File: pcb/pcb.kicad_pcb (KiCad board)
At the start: 2 copper layers, 234.7 x 91.6 mm, 95 parts, among them J1 USB_C_Receptacle_USB2.0, Q1 DTC123J, SW1 SW_Push, SW10 SW_PUSH, SW11 SW_PUSH, SW12 SW_PUSH, SW13 SW_PUSH, SW14 SW_PUSH, SW15 SW_PUSH, SW16 SW_PUSH, SW17 SW_PUSH, SW18 SW_PUSH, SW19 SW_PUSH, SW2 SW_PUSH, SW20 SW_PUSH, SW21 SW_PUSH, SW22 SW_PUSH, SW23 SW_PUSH, SW24 SW_PUSH, SW25 SW_PUSH, SW26 SW_PUSH, SW27 SW_PUSH, SW28 SW_PUSH, SW29 SW_PUSH, SW3 SW_PUSH, SW30 SW_PUSH, SW31 SW_PUSH, SW32 SW_PUSH, SW33 SW_PUSH, SW34 Rotary_Encoder_Switch, SW4 SW_PUSH, SW5 SW_PUSH, SW6 SW_PUSH, SW7 SW_PUSH, SW8 SW_PUSH, SW9 SW_PUSH, U1 STM32F072CBTx, U2 MCP1700-3002E_SOT23, U3 SRV05-4

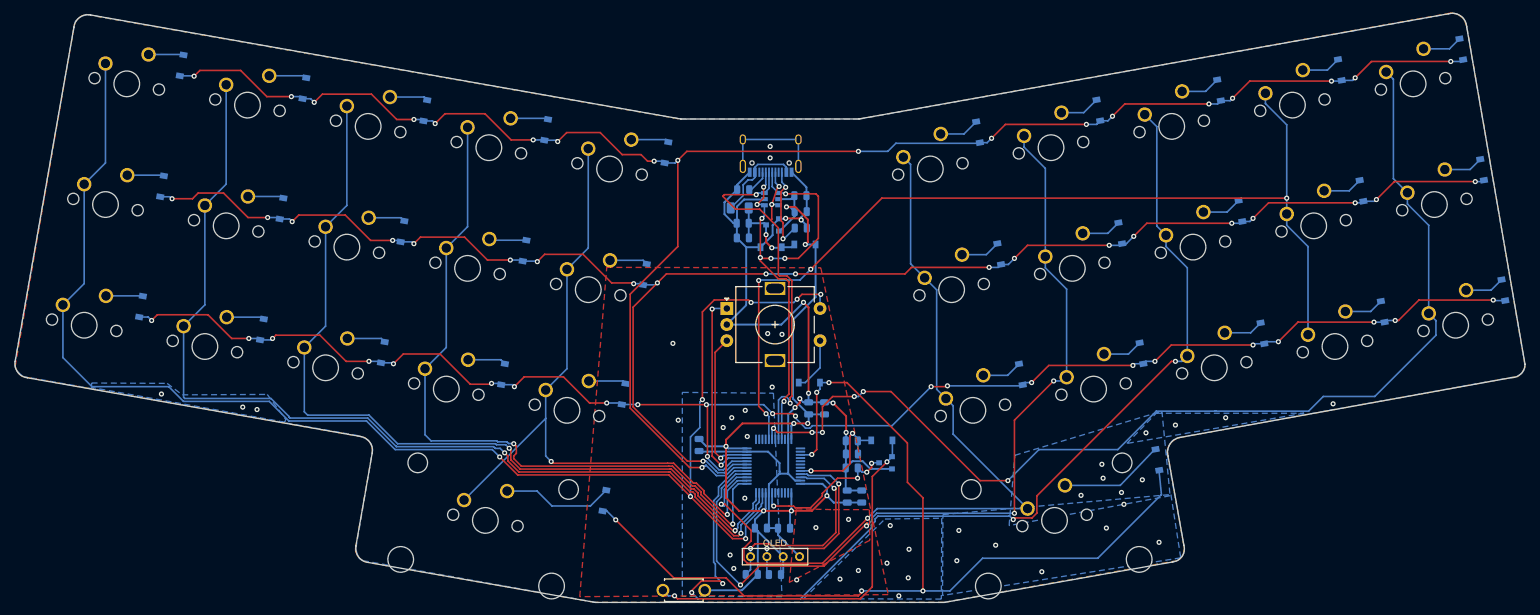
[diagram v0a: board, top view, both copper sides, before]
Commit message: Finishes reroute
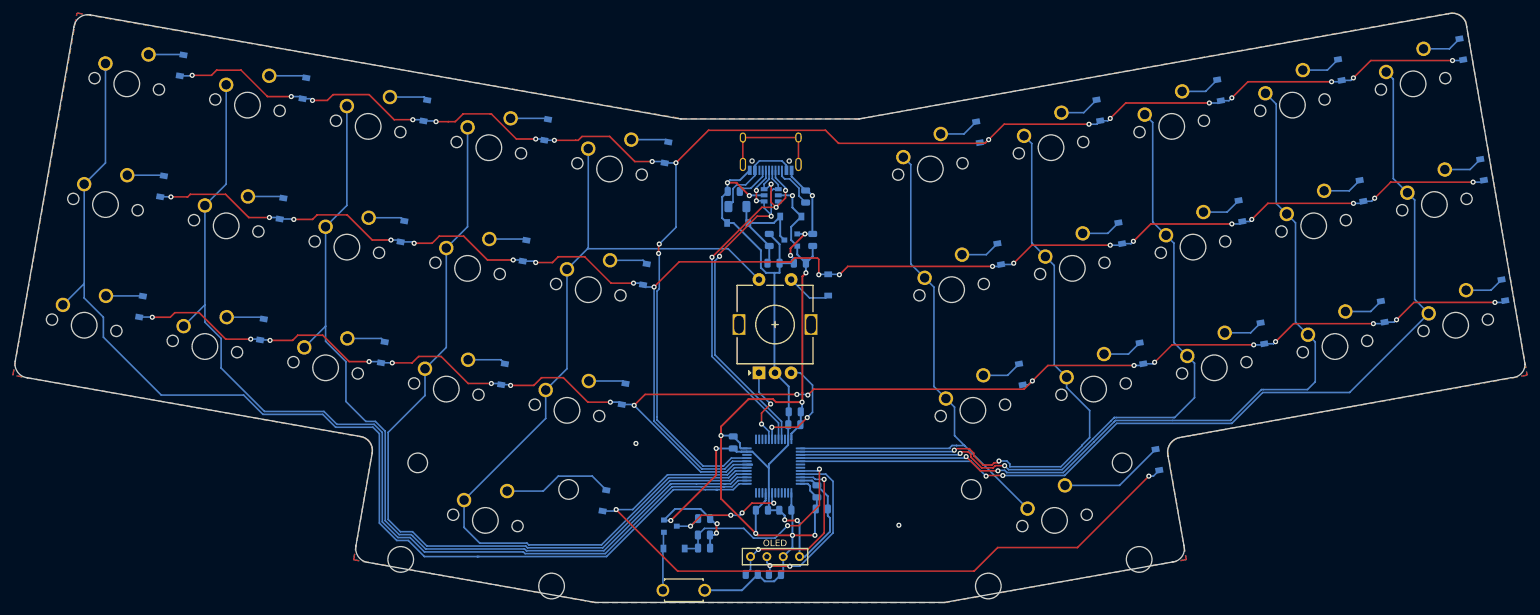
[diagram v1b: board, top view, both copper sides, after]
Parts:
- moved D35 36.4 mm to (124.0, 155.0), turned to 180 degrees
- moved Q1 34.9 mm to (123.4, 151.5), turned to 0 degrees
- moved C10 28.4 mm to (128.7, 154.9), turned to 0 degrees
- moved R3 26.2 mm to (128.6, 152.8), turned to 0 degrees
- moved C11 24.3 mm to (128.7, 150.3), turned to 0 degrees
- moved D33 15.5 mm to (148.0, 114.0), turned to 90 degrees
- moved C8 10.5 mm to (143.6, 110.6), turned to 180 degrees
- moved C9 7.84 mm to (139.5, 110.6), turned to 0 degrees
- moved C5 6.51 mm to (147.0, 148.8), turned to 0 degrees
- moved D36 6.41 mm to (133.9, 104.3)
- moved C7 5.33 mm to (133.2, 138.5)
- moved R4 4.96 mm to (144.4, 100.2), turned to 270 degrees
- moved D34 4.87 mm to (142.2, 103.3)
- moved C6 4.78 mm to (146.2, 146.1)
- moved R2 4.78 mm to (145.6, 107.0), turned to 90 degrees
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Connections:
- D33 pad 1: row3 -> Net-(D33-Pad1)
- D33 pad 2: Net-(D33-Pad2) -> row1
- J1 pad A8: Net-(J1-PadA8) -> (no net)
- J1 pad B8: Net-(J1-PadB8) -> (no net)
- SW34 pad S1: Net-(D33-Pad2) -> Net-(D33-Pad1)
- SW34 pad S2: col0 -> col4
- U1 pad 10: col0 -> (no net)
- U1 pad 11: col1 -> (no net)
- U1 pad 12: col2 -> (no net)
- U1 pad 13: col3 -> col0
- U1 pad 14: col4 -> col1
- U1 pad 15: col5 -> col2
- U1 pad 16: col6 -> col3
- U1 pad 17: col7 -> col4
- U1 pad 18: row0 -> row3
- U1 pad 19: row1 -> row2
- U1 pad 2: Net-(U1-Pad2) -> (no net)
- U1 pad 20: row2 -> row1
- U1 pad 21: enc_a -> row0
- U1 pad 22: enc_b -> (no net)
- U1 pad 25: Net-(U1-Pad25) -> (no net)
- U1 pad 26: Net-(U1-Pad26) -> (no net)
- U1 pad 27: Net-(U1-Pad27) -> (no net)
- U1 pad 28: Net-(U1-Pad28) -> (no net)
- U1 pad 29: col8 -> enc_a
- U1 pad 3: Net-(U1-Pad3) -> (no net)
- U1 pad 30: col9 -> enc_b
- U1 pad 31: Net-(U1-Pad31) -> (no net)
- U1 pad 34: Net-(U1-Pad34) -> (no net)
- U1 pad 37: Net-(U1-Pad37) -> col5
- U1 pad 38: Net-(U1-Pad38) -> col6
- U1 pad 39: row3 -> col7
- U1 pad 4: Net-(U1-Pad4) -> (no net)
- U1 pad 40: Net-(U1-Pad40) -> col8
- U1 pad 41: Net-(U1-Pad41) -> col9
- U1 pad 42: Net-(U1-Pad42) -> (no net)
- U1 pad 43: Net-(U1-Pad43) -> (no net)
- U1 pad 5: Net-(U1-Pad5) -> (no net)
- U1 pad 6: Net-(U1-Pad6) -> (no net)
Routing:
- net Net-(D35-Pad2): track 57.9 -> 9.08 mm, vias 2 -> 0
- net col0: track 226.0 -> 177.3 mm, vias 7 -> 0
- net col7: track 163.1 -> 115.0 mm, vias 4 -> 2
- net col5: track 129.2 -> 88.3 mm, vias 2 -> 0
- net row3: track 157.7 -> 120.1 mm, vias 6 -> 2
- net col4: track 108.1 -> 145.4 mm, vias 2 -> 0
- net col6: track 135.6 -> 100.4 mm, vias 4 -> 2
- net col9: track 169.5 -> 149.3 mm, vias 6 -> 2
- net enc_a: track 31.6 -> 12.1 mm
- net col8: track 153.0 -> 135.1 mm, vias 4 -> 2
- net BOOT0: track 18.7 -> 34.9 mm
- net +3V3: track 153.7 -> 138.5 mm, vias 8 -> 7
- net col3: track 114.5 -> 128.7 mm, vias 2 -> 0
- net D-: track 73.3 -> 61.7 mm, vias 8 -> 4
- net Net-(D33-Pad2): track 8.49 -> 0.00 mm
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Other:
- rule pad_to_mask_clearance: 0.051 -> 0
